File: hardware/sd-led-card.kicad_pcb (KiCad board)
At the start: 2 copper layers, 24 x 16 mm, 12 parts, among them J1 SD card edge contacts, U1 RP2350A

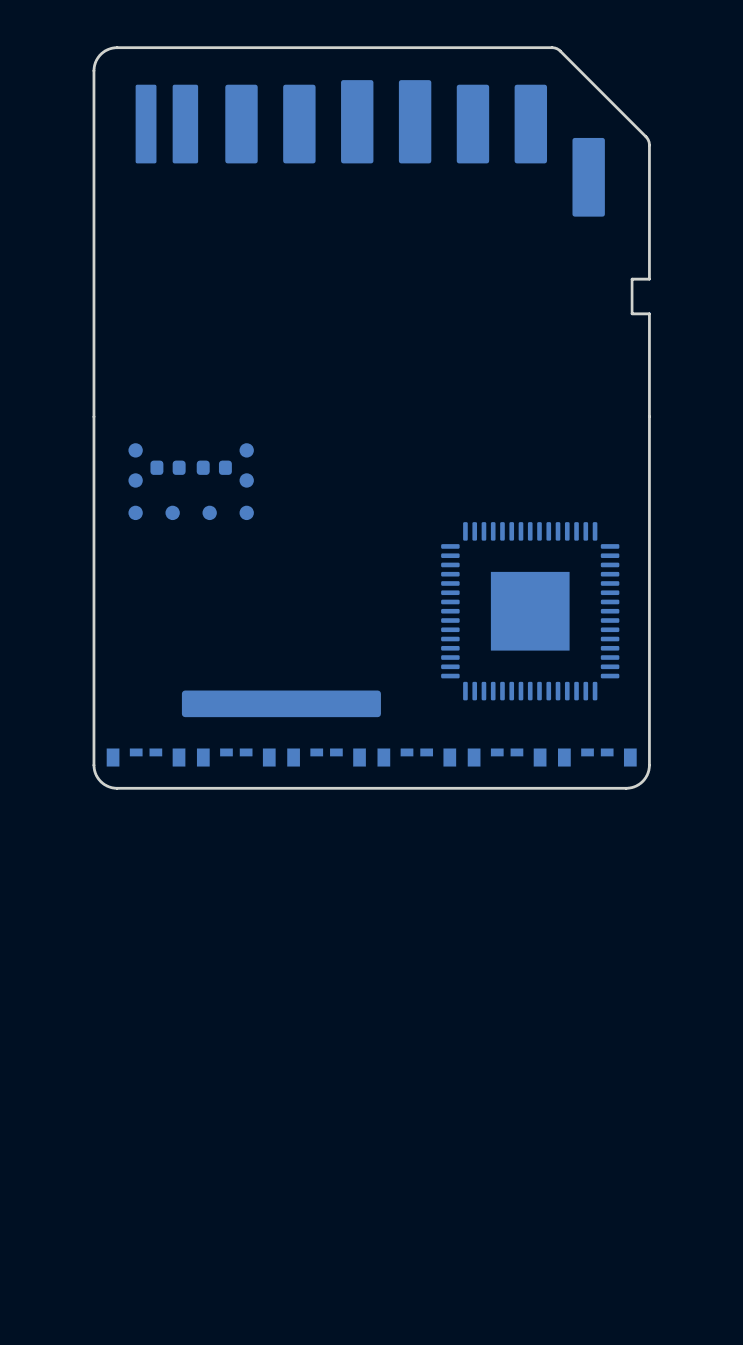
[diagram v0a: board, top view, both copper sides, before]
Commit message: Add breakaway SD probe tail
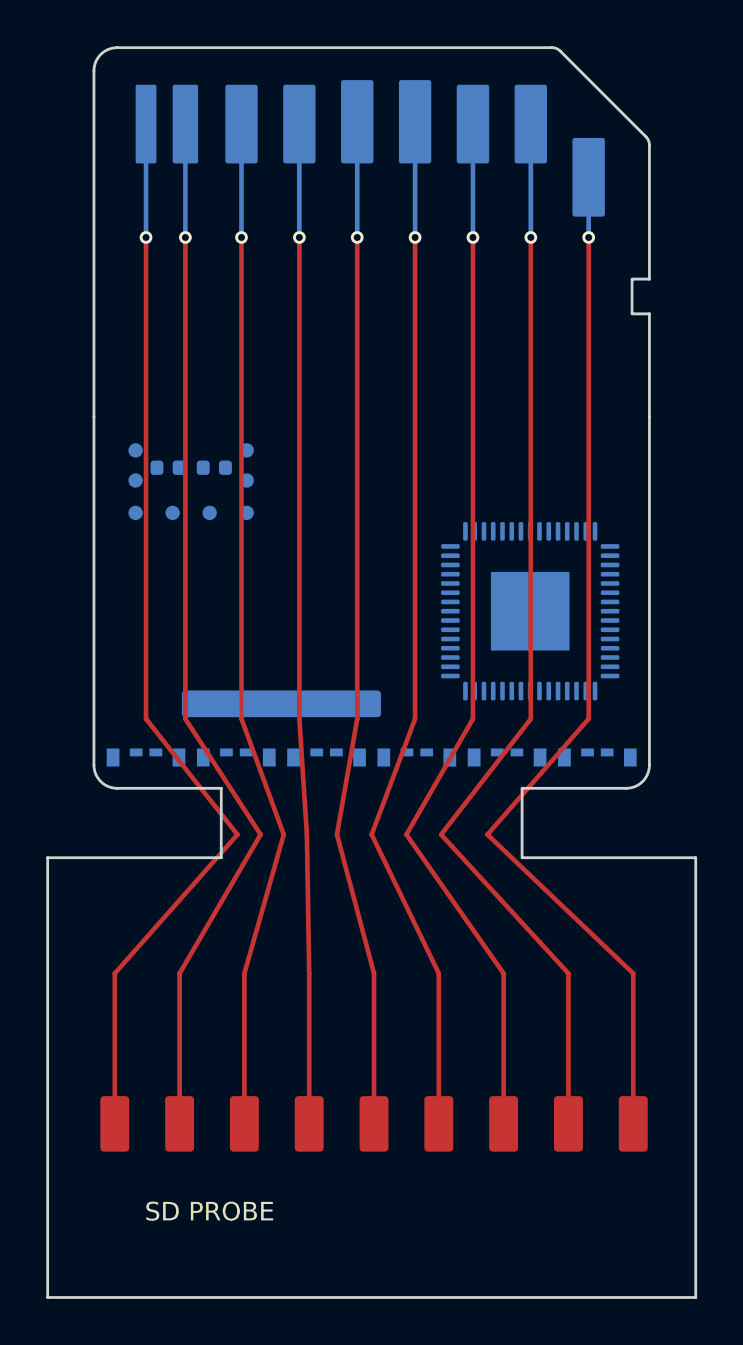
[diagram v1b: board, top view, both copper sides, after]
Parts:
- added J2: breakaway SD probe pads, , F.Cu at (0.00, 0.00)
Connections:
- J1 pad 1: (no net) -> SD_DAT2
- J1 pad 2: (no net) -> SD_DAT3
- J1 pad 3: (no net) -> SD_CMD
- J1 pad 4: (no net) -> +3V3
- J1 pad 5: (no net) -> SD_CLK
- J1 pad 6: (no net) -> GND
- J1 pad 7: (no net) -> SD_DAT0
- J1 pad 8: (no net) -> SD_DAT1
- J1 pad 9: (no net) -> SD_VSS2
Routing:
- net SD_DAT2: track 0.00 -> 43.9 mm, vias 0 -> 1
- net SD_DAT1: track 0.00 -> 43.8 mm, vias 0 -> 1
- net SD_VSS2: track 0.00 -> 42.5 mm, vias 0 -> 1
- net SD_DAT3: track 0.00 -> 42.5 mm, vias 0 -> 1
- net SD_DAT0: track 0.00 -> 42.3 mm, vias 0 -> 1
- net SD_CMD: track 0.00 -> 41.4 mm, vias 0 -> 1
- net GND: track 0.00 -> 41.0 mm, vias 0 -> 1
- net +3V3: track 0.00 -> 40.7 mm, vias 0 -> 1
- net SD_CLK: track 0.00 -> 40.4 mm, vias 0 -> 1
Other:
- board size 24 x 16 mm -> 28 x 38 mm
- board text added: "SD PROBE"
